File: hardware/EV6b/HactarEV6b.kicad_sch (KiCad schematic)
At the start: 110 parts, among them J1 Conn_01x02_Female, J10 Conn_01x08_Female, J11 Conn_01x06_Female, J12 Conn_01x04_Female, J13 Conn_01x04_Female, J14 Conn_01x04_Female, J15 Conn_01x02_Female, J2 Conn_01x02_Female, J3 Conn_01x04_Female, J4 Conn_01x08_Male, J5 Conn_01x04_Female, J6 Conn_01x04_Female, J7 Conn_01x04_Female, J8 Conn_01x06_Female, J9 USB_C_Receptacle, SW1 SW_Push, SW2 SW_Push, SW3 SW_Push, U1 STM32F446RET6, U11 ESP32-S3-WROOM-1-N8R2, U12 MCP73832-2-OT, U13 BM14B(0.8)-24DS-0.4V(53), U2 AMS1117-3.3, U3 CH340C, U4 USBLC6-2P6, U5 STM32F091CCT6, U6 WM8960CGEFL/RV, Y1 Crystal_GND24

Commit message: move to new name and add LCSC part numbers
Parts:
- 120R1: JLC (none) -> 0603; LCSC (none) -> C127301
- C1, C19: LCSC (none) -> C23733
- C10: LCSC (none) -> C142376
- C11: LCSC (none) -> C338032
- C2: LCSC (none) -> C703069
- C21: LCSC (none) -> C76594
- C23, C4: value 33P -> 33p; JLC (none) -> 0805; LCSC (none) -> C1663
- C28, C3, C31, C6: value 4.7u -> 4u7; LCSC (none) -> C159984
- C29, C30: value 100U -> 100u; JLC (none) -> 1206; LCSC (none) -> C87164
- C5: JLC (none) -> 0402; LCSC (none) -> C87148
- C7, D10, D2: LCSC (none) -> C191023
- C8: LCSC (none) -> C361206
- C9: JLC (none) -> 0402; LCSC (none) -> C142376
- CR1: LCSC (none) -> C83836
- D11: LCSC (none) -> C130114
- D18, D3: LCSC (none) -> C2927824
- J1: LCSC (none) -> C295747
- J10: LCSC (none) -> C265121; now left out of the parts list
- J11, J8: LCSC (none) -> C265405
- J12, J3: LCSC (none) -> C3029343
- J4: LCSC (none) -> C5156616; now not fitted; now left out of the parts list
- J9: LCSC (none) -> C165948
- R1: LCSC (none) -> C82453
- R11: value 150 -> 150r; LCSC (none) -> C186306
- R12, R14, R15, R17, R18, R24, R25, R34, R35: value 150 -> 150r
- R13, R6: value 180 -> 180r; LCSC (none) -> C186119
- R16, R23, R33: value 180 -> 180r
- R2: LCSC (none) -> C325521
- R20, R7: LCSC (none) -> C144053
- R22: value 330 -> 330r; LCSC (none) -> C105876
- R26, R27, R28, R29, R30, R31: value 330 -> 330r
- R36: LCSC (none) -> C279981
- R37: LCSC (none) -> C258126
- R38: LCSC (none) -> C409612
- R39: LCSC (none) -> C131617
- R4: LCSC (none) -> C409670
- R40, R41: value 1R0 -> 1r0; JLC (none) -> 0402; LCSC (none) -> C881335
- R9: LCSC (none) -> C102890
- SW1: LCSC (none) -> C266189
- U1: LCSC (none) -> C69336
- U11: Availability In Stock -> (none); LCSC (none) -> C3013944; Package - Espressif Systems -> (none); Price None -> (none); Purchase-URL https://pricing.snapeda.com/search/part/ESP32-S3-WROOM-1-N8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 -> (none)
- U12: LCSC (none) -> C424093
- U13: footprint (none) -> BM14B(0.B)-24DS-0:BM14B(0.B)-24DS-0.4V(53); LCSC (none) -> C3640874; now left out of the parts list
- U2: LCSC (none) -> C351784
- U3: LCSC (none) -> C84681
- U4: LCSC (none) -> C2827693
- U6: LCSC (none) -> C18752; now left out of the parts list
- Y1: LCSC (none) -> C13738
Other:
- note added: "Display - 2.54MM T"
- note removed: "Display - 2MM T"
- moved on the sheet: J12, J6

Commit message: changing USB connector started
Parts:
- D4, D5: LCSC (none) -> C2927824
- J13: LCSC (none) -> C3029343
- J15, J2: LCSC (none) -> C295747
- J9: footprint Connector_USB:USB_C_Receptacle_HRO_TYPE-C-31-M-12 -> PartLibrary:USB_C_Receptacle_HRO_TYPE-C-31-M-13; LCSC C165948 -> C223906
- R11: LCSC C186306 -> C25143
- R13, R6: LCSC C186119 -> C966703
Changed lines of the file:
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@@
       (effects (font (size 1.27 1.27)) (justify right))
     )
-    (property "Footprint" "Connector_USB:USB_C_Receptacle_HRO_TYPE-C-31-M-12" (at 48.26 203.2 0)
+    (property "Footprint" "PartLibrary:USB_C_Receptacle_HRO_TYPE-C-31-M-13" (at 48.26 203.2 0)
       (effects (font (size 1.27 1.27)) hide)
     )
@@
       (effects (font (size 1.27 1.27)) hide)
     )
-    (property "LCSC" "C165948" (at 52.07 203.2 0)
+    (property "LCSC" "C223906" (at 52.07 203.2 0)
       (effects (font (size 1.27 1.27)) hide)
     )
@@
       (effects (font (size 1.27 1.27)) hide)
     )
+    (property "LCSC" "C2927824" (at 273.05 50.8 0)
+      (effects (font (size 1.27 1.27)) hide)
+    )
     (pin "1")
     (pin "2")
@@
       (effects (font (size 1.27 1.27)) hide)
     )
+    (property "LCSC" "C295747" (at 483.87 38.1 0)
+      (effects (font (size 1.27 1.27)) hide)
+    )
     (pin "1")
     (pin "2")
@@
       (effects (font (size 1.27 1.27)) hide)
     )
+    (property "LCSC" "C2927824" (at 426.72 45.72 0)
+      (effects (font (size 1.27 1.27)) hide)
+    )
     (pin "1")
     (pin "2")
@@
       (effects (font (size 1.27 1.27)) hide)
     )
+    (property "LCSC" "C295747" (at 344.17 233.68 0)
+      (effects (font (size 1.27 1.27)) hide)
+    )
     (pin "1")
     (pin "2")
@@
       (effects (font (size 1.27 1.27)) hide)
     )
-    (property "LCSC" "C186119" (at 125.73 74.93 90)
+    (property "LCSC" "C966703" (at 125.73 74.93 90)
       (effects (font (size 1.27 1.27)) hide)
     )
@@
       (effects (font (size 1.27 1.27)) hide)
     )
-    (property "LCSC" "C186306" (at 125.73 48.26 90)
+    (property "LCSC" "C25143" (at 125.73 48.26 90)
       (effects (font (size 1.27 1.27)) hide)
     )
@@
       (effects (font (size 1.27 1.27)) hide)
     )
+    (property "LCSC" "C3029343" (at 392.43 233.68 0)
+      (effects (font (size 1.27 1.27)) hide)
+    )
     (pin "1")
     (pin "2")
@@
       (effects (font (size 1.27 1.27)) (justify left bottom) hide)
     )
-    (property "Description" "\\nWiFi 802.11a/b/g/n, Bluetooth v5.0 Transceiver Module 2.4GHz Antenna Not Included -\\n" (at 215.9 91.44 0)
+    (property "Description" "WiFi 802.11a/b/g/n, Bluetooth v5.0 Transceiver Module 2.4GHz Antenna Not Included" (at 215.9 91.44 0)
       (effects (font (size 1.27 1.27)) (justify left bottom) hide)
     )
@@
       (effects (font (size 1.27 1.27)) hide)
     )
-    (property "LCSC" "C186119" (at 125.73 53.34 90)
+    (property "LCSC" "C966703" (at 125.73 53.34 90)
       (effects (font (size 1.27 1.27)) hide)
     )

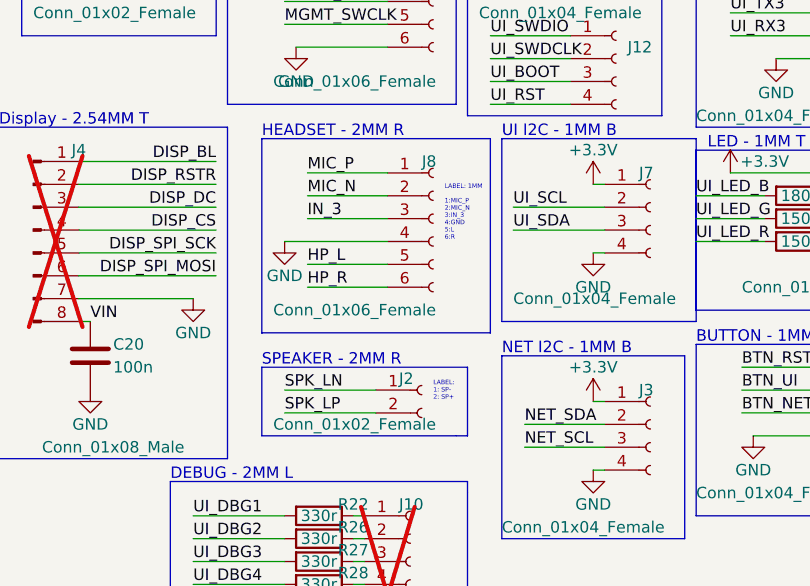
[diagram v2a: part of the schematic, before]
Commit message: move to new USB connector
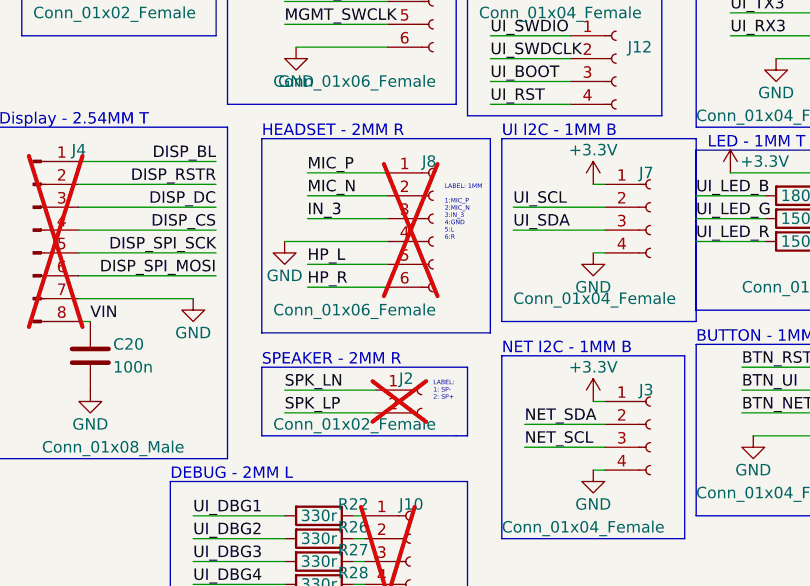
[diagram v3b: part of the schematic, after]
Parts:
- J2, J8: now not fitted; now left out of the parts list
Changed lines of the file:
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@@
   )
   (symbol (lib_id "Connector:Conn_01x02_Female") (at 344.17 233.68 0) (unit 1)
-    (in_bom yes) (on_board yes) (dnp no)
+    (in_bom no) (on_board yes) (dnp yes)
     (property "Reference" "J2" (at 341.63 232.41 0)
       (effects (font (size 1.27 1.27)) (justify left))
@@
   )
   (symbol (lib_id "Connector:Conn_01x06_Female") (at 345.44 214.63 0) (unit 1)
-    (in_bom yes) (on_board yes) (dnp no)
+    (in_bom no) (on_board yes) (dnp yes)
     (property "Reference" "J8" (at 344.17 208.28 0)
       (effects (font (size 1.27 1.27)) (justify left))
